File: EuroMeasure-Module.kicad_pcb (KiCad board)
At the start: 2 copper layers, 99.9 x 99.9 mm, 47 parts, among them SW1 RESET, SW2 ADR, U1 AMS1117-3.3, U2 STM32G030CxT, Y1 NX2520 16MHz

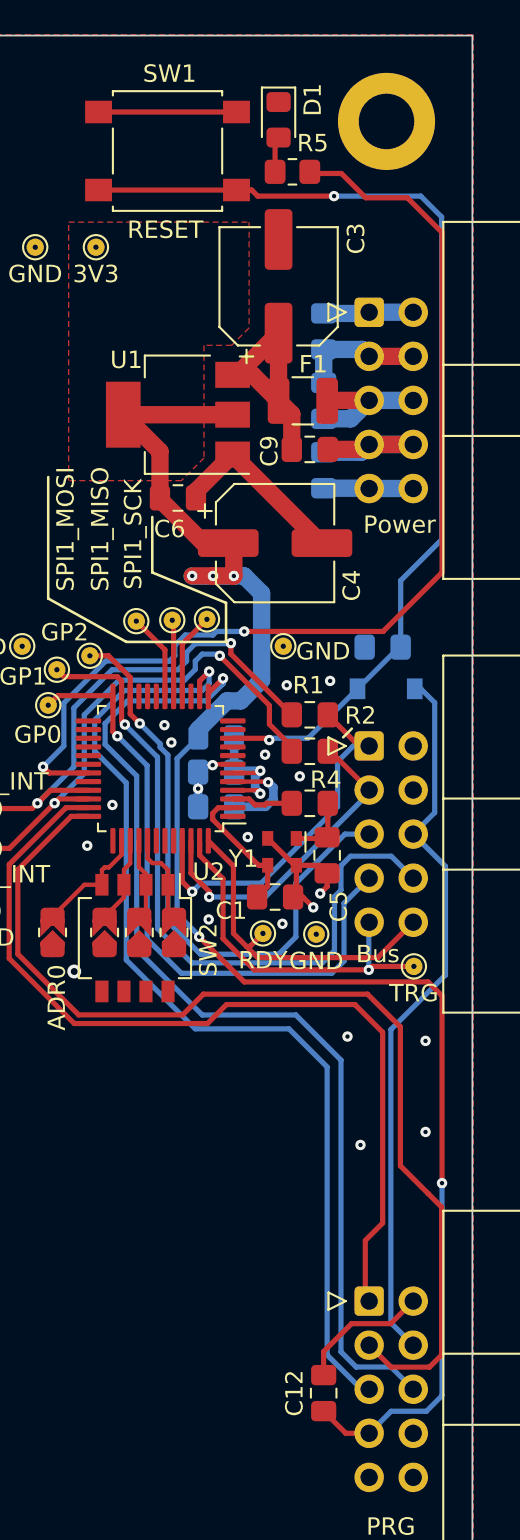
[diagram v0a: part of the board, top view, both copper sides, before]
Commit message: Fixed xtal connection
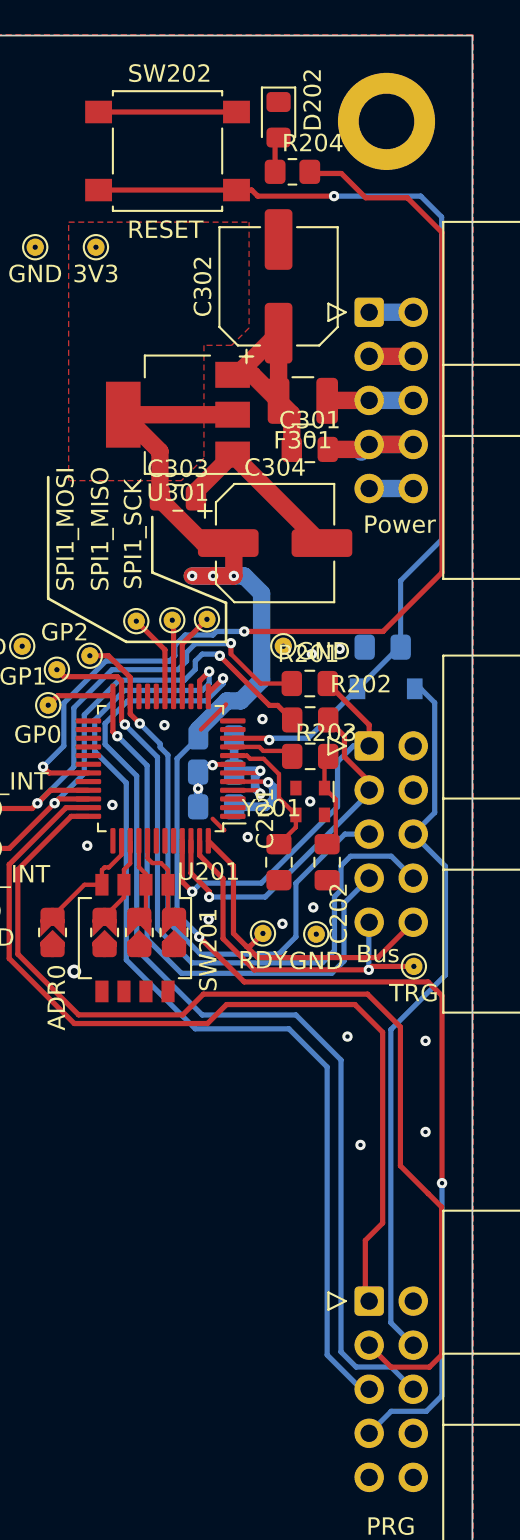
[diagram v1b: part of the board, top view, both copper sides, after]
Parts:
- removed C12, C13, C14, C15, C6, C9: 10u, Capacitor_SMD:C_0805_2012Metric_Pad1.18x1.45mm_HandSolder
- removed C3, C4: 220u, Capacitor_SMD:CP_Elec_6.3x7.7
- removed F1: Polyfuse, Fuse:Fuse_1210_3225Metric
- removed TP16: 3V3, MEMS_Custom:TestPoint_Pad_D1.0mm
- removed U1: AMS1117-3.3, Package_TO_SOT_SMD:SOT-223-3_TabPin2
- added C301: 10u, Capacitor_SMD:C_0805_2012Metric_Pad1.18x1.45mm_HandSolder, F.Cu at (186.8, 74.0)
- added C302: 220u, Capacitor_SMD:CP_Elec_6.3x7.7, F.Cu at (185.0, 64.6)
- added C303: 10u, Capacitor_SMD:C_0805_2012Metric_Pad1.18x1.45mm_HandSolder, F.Cu at (179.2, 76.8)
- added C304: 220u, Capacitor_SMD:CP_Elec_6.3x7.7, F.Cu at (184.8, 79.4)
- added F301: Polyfuse, Fuse:Fuse_1210_3225Metric, F.Cu at (186.4, 71.2)
- added TP301: 3V3, MEMS_Custom:TestPoint_Pad_D1.0mm, F.Cu at (174.5, 62.3)
- added U301: AMS1117-3.3, Package_TO_SOT_SMD:SOT-223-3_TabPin2, F.Cu at (179.2, 72.0)
- moved Y201 3.33 mm to (186.8, 94.3)
- moved R203 2.71 mm to (186.8, 91.7)
- moved C201 2.02 mm to (185.0, 97.8), turned to -90 degrees
- moved R202 1.81 mm to (186.8, 89.6)
- moved R201 1.80 mm to (186.8, 87.5)
- moved C202 0.39 mm to (187.8, 97.8)
- renumbered B1 to B201, C1 to C201, C5 to C202, C2 to C203, C7 to C204, C8 to C205, D2 to D201, D1 to D202, JP1 to JP201, JP2 to JP202, JP3 to JP203, JP4 to JP204, L1 to L201, R1 to R201, R2 to R202, R4 to R203, R5 to R204, SW2 to SW201, SW1 to SW202, TP11 to TP201, TP12 to TP202, TP13 to TP203, TP14 to TP204, TP15 to TP205, TP1 to TP206, TP2 to TP207, TP3 to TP208, TP4 to TP209, TP5 to TP210, TP6 to TP211, TP7 to TP212, TP8 to TP213, TP9 to TP214, TP10 to TP215, U2 to U201, Y1 to Y201
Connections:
- net +15V renamed 15V_INPUT
- net +5V renamed 5V_INPUT
- net -15V renamed -15V_INPUT
- net /ADR0 renamed /EuroMeasure/ADR0
- net /ADR1 renamed /EuroMeasure/ADR1
- net /ADR2 renamed /EuroMeasure/ADR2
- net /ADR3 renamed /EuroMeasure/ADR3
- net /GP0 renamed /EuroMeasure/GP0
- net /GP1 renamed /EuroMeasure/GP1
- net /GP2 renamed /EuroMeasure/GP2
- net /PA0 renamed /EuroMeasure/PA0
- net /PA1 renamed /EuroMeasure/PA1
- net /PA10 renamed /EuroMeasure/PA10
- net /PA15 renamed /EuroMeasure/PA15
- net /PA4 renamed /EuroMeasure/PA4
- net /PA8 renamed /EuroMeasure/PA8
- net /PA9 renamed /EuroMeasure/PA9
- net /PB0 renamed /EuroMeasure/PB0
- net /PB1 renamed /EuroMeasure/PB1
- net /PB2 renamed /EuroMeasure/PB2
- net /PB3 renamed /EuroMeasure/PB3
- net /PB4 renamed /EuroMeasure/PB4
- net /PB5 renamed /EuroMeasure/PB5
- net /PC13 renamed /EuroMeasure/PC13
- net /PC6 renamed /EuroMeasure/PC6
- net /RDY renamed /EuroMeasure/RDY
- net /RST renamed /EuroMeasure/RST
- net /RX_DEBUG renamed /EuroMeasure/RX_DEBUG
- net /SCL_EXT renamed /EuroMeasure/SCL_EXT
- net /SCL_INT renamed /EuroMeasure/SCL_INT
- net /SDA_EXT renamed /EuroMeasure/SDA_EXT
- net /SDA_INT renamed /EuroMeasure/SDA_INT
- net /SPI1_MISO renamed /EuroMeasure/SPI1_MISO
- net /SPI1_MOSI renamed /EuroMeasure/SPI1_MOSI
- net /SPI1_SCK renamed /EuroMeasure/SPI1_SCK
- net /SPI2_MISO renamed /EuroMeasure/SPI2_MISO
- net /SPI2_MOSI renamed /EuroMeasure/SPI2_MOSI
- net /SPI2_SCK renamed /EuroMeasure/SPI2_SCK
- net /SWCLK renamed /EuroMeasure/SWCLK
- net /SWDIO renamed /EuroMeasure/SWDIO
- net /TRG renamed /EuroMeasure/TRG
- net /TX_DEBUG renamed /EuroMeasure/TX_DEBUG
- C201 pad 1: Net-(C1-Pad1) -> Net-(C201-Pad1)
- R203 pad 2: Net-(R4-Pad2) -> Net-(R203-Pad2)
- U201 pad 2: Net-(C1-Pad1) -> unconnected-(U201-Pad2)
- U201 pad 3: Net-(R4-Pad2) -> unconnected-(U201-Pad3)
- U201 pad 8: /PF0 -> Net-(C201-Pad1)
- U201 pad 9: /PF1 -> Net-(R203-Pad2)
- Y201 pad 3: Net-(C1-Pad1) -> Net-(C201-Pad1)
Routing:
- net GND: track 56.0 -> 36.5 mm, vias 20 -> 18
- net Net-(C3-Pad1): track 13.9 -> 0.00 mm
- net +5V: track 0.00 -> 13.9 mm
- net Net-(C1-Pad1): track 8.00 -> 0.00 mm
- net Net-(C201-Pad1): track 0.00 -> 7.95 mm
- net Net-(R203-Pad2): track 0.00 -> 3.65 mm
- net Net-(R4-Pad2): track 3.58 -> 0.00 mm
- net +3.3V: track 95.4 -> 92.2 mm
- net 5V_INPUT: track 8.04 -> 4.97 mm
- net 15V_INPUT: track 5.17 -> 2.56 mm
- net -15V_INPUT: track 5.19 -> 2.64 mm
- net /EuroMeasure/SCL_EXT: track 21.5 -> 23.5 mm
- net Net-(C202-Pad1): track 3.78 -> 5.77 mm
- net /EuroMeasure/SDA_EXT: track 18.9 -> 20.6 mm
- net /EuroMeasure/SDA_INT: track 29.5 -> 28.0 mm
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
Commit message: Fixed programmer reset
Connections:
- B201 pad 24: /EuroMeasure/RST -> /EuroMeasure/LOCAL_RST
- C203 pad 1: Net-(C203-Pad1) -> /EuroMeasure/LOCAL_RST
- D201 pad 2: Net-(C203-Pad1) -> /EuroMeasure/LOCAL_RST
- SW202 pad 2: Net-(C203-Pad1) -> /EuroMeasure/LOCAL_RST
- U201 pad 10: Net-(C203-Pad1) -> /EuroMeasure/LOCAL_RST
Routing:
- net /EuroMeasure/LOCAL_RST: track 0.00 -> 101.3 mm, vias 0 -> 2
- net Net-(C203-Pad1): track 58.1 -> 0.00 mm, vias 2 -> 0
- net /EuroMeasure/RST: track 41.6 -> 9.57 mm

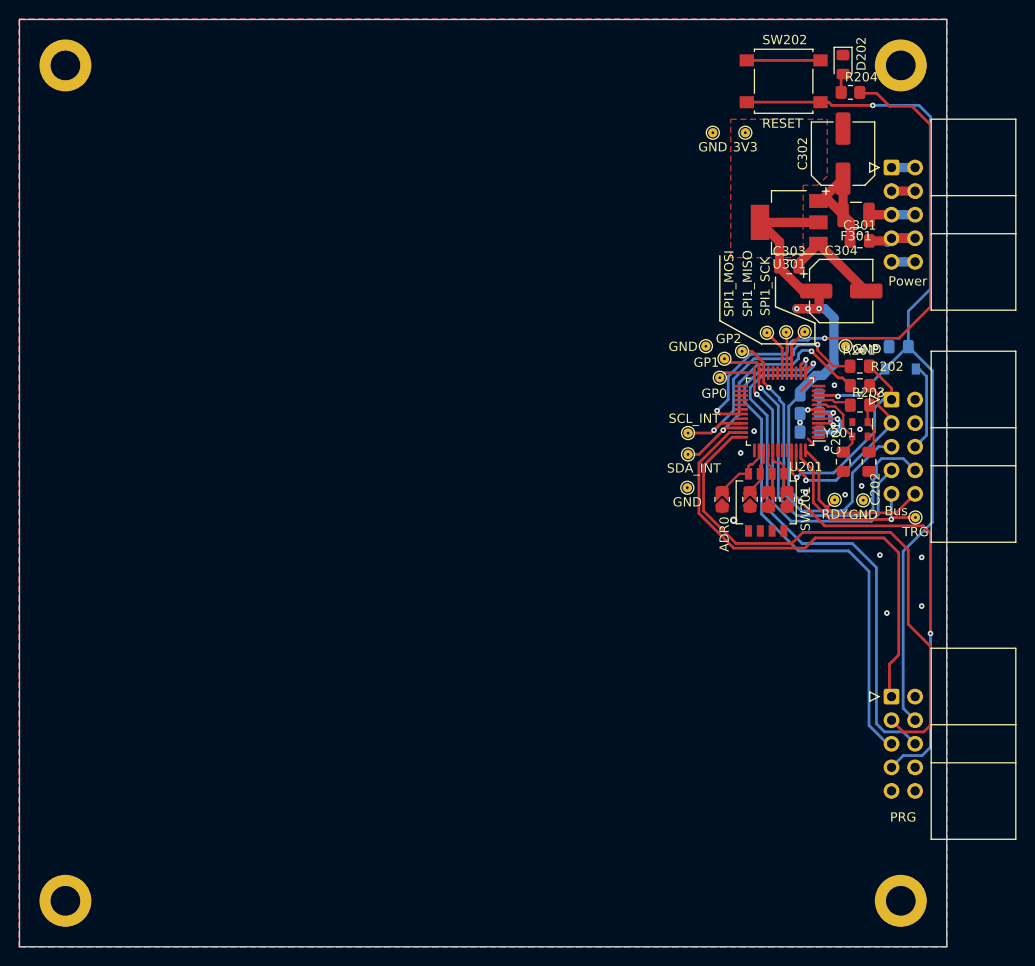
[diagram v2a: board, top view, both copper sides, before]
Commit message: Updated PCB to current standards
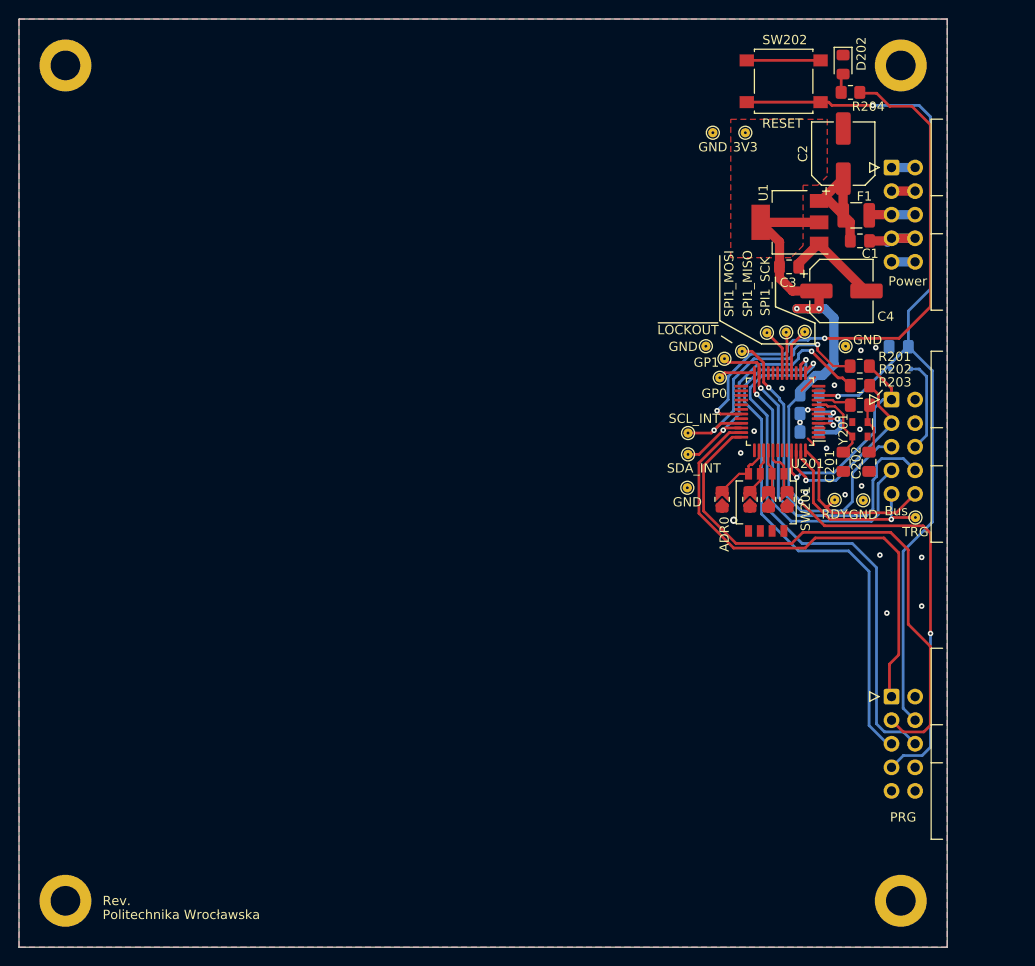
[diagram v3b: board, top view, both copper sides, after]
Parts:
- removed C301, C303: 10u, Capacitor_SMD:C_0805_2012Metric_Pad1.18x1.45mm_HandSolder
- removed C302, C304: 220u, Capacitor_SMD:CP_Elec_6.3x7.7
- removed F301: Polyfuse, Fuse:Fuse_1210_3225Metric
- removed TP301: 3V3, MEMS_Custom:TestPoint_Pad_D1.0mm
- removed U301: AMS1117-3.3, Package_TO_SOT_SMD:SOT-223-3_TabPin2
- added C1: 10u, Capacitor_SMD:C_0805_2012Metric_Pad1.18x1.45mm_HandSolder, F.Cu at (186.8, 74.0)
- added C2: 220u, Capacitor_SMD:CP_Elec_6.3x7.7, F.Cu at (185.0, 64.6)
- added C3: 10u, Capacitor_SMD:C_0805_2012Metric_Pad1.18x1.45mm_HandSolder, F.Cu at (179.2, 76.8)
- added C4: 220u, Capacitor_SMD:CP_Elec_6.3x7.7, F.Cu at (184.8, 79.4)
- added F1: Polyfuse, Fuse:Fuse_1210_3225Metric, F.Cu at (186.4, 71.2)
- added TP1: 3V3, MEMS_Custom:TestPoint_Pad_D1.0mm, F.Cu at (174.5, 62.3)
- added U1: AZ1117-3V3, Package_TO_SOT_SMD:SOT-223-3_TabPin2, F.Cu at (179.3, 72.0)
- D201: footprint Diode_SMD:D_SOD-123 -> Diode_SMD:D_SOD-323F
- TP213: value GP2 -> ~{LOCKOUT}
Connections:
- net /EuroMeasure/GP2 renamed /EuroMeasure/~{LOCKOUT}
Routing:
- net GND: track 36.5 -> 35.5 mm
- net +3.3V: track 92.2 -> 92.9 mm
- net /EuroMeasure/SCL_EXT: track 23.5 -> 23.0 mm
- net /EuroMeasure/RST: track 9.57 -> 10.1 mm
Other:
- board size 99.9 x 99.9 mm -> 100 x 100 mm
